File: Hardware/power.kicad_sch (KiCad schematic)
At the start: 48 parts, among them J1 USB4110GFA, Q1 AO3407A, U1 TPS54302, U2 USBLC6-2SC6, U3 INA226, U4 AP63205WU, U5 AP2112K-3.3, U6 AP7343-33W5-7

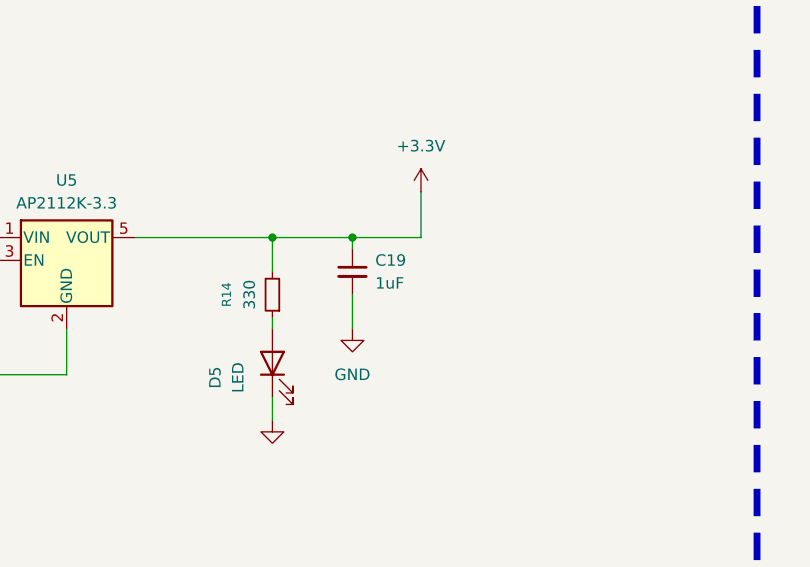
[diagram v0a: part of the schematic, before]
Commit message: fixed caps values
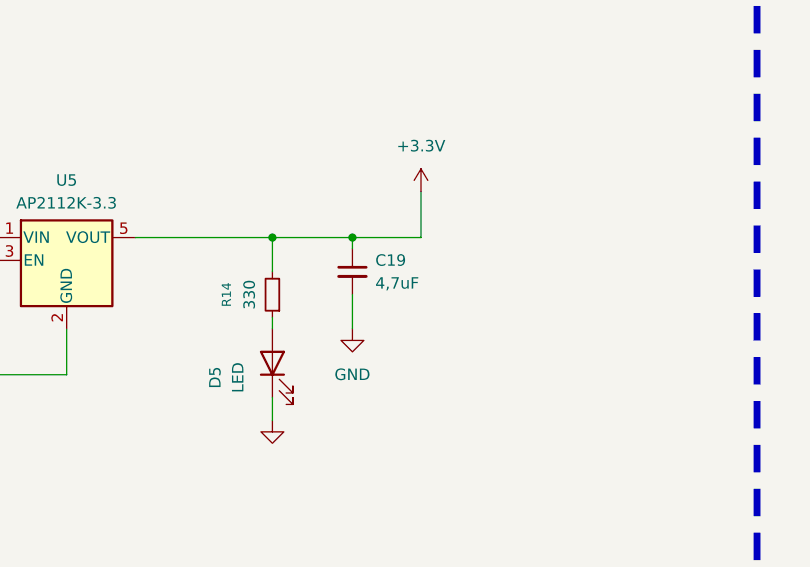
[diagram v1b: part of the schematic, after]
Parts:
- C19: value 1uF -> 4,7uF
